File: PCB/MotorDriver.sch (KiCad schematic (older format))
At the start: 5 parts, among them U1 DRV8871DDA

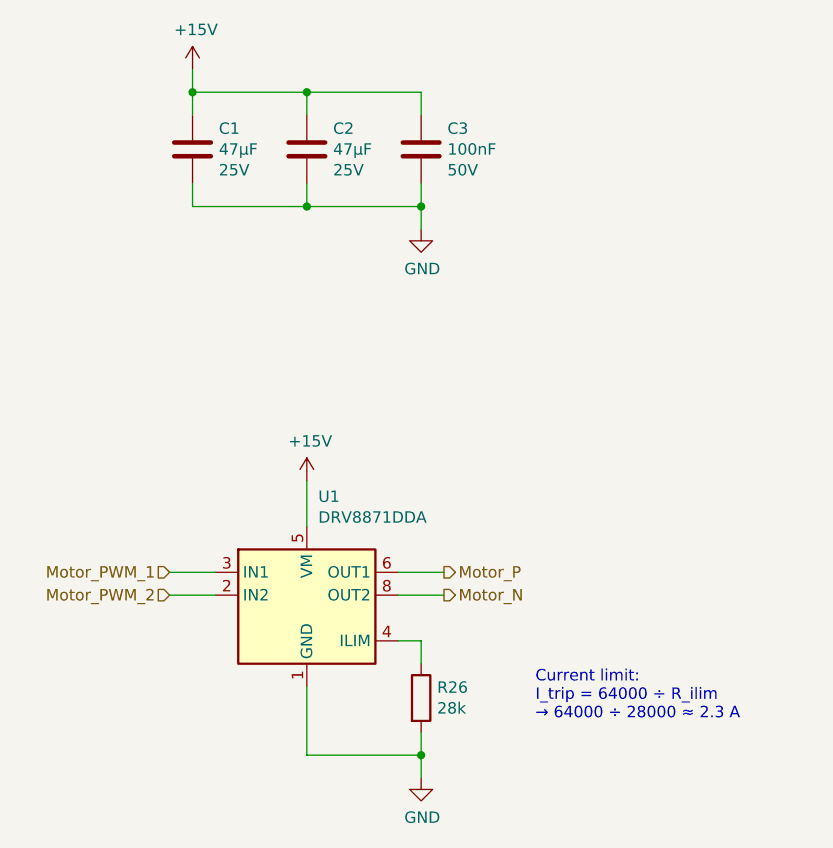
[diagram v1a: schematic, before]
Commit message: Add support for the weight sensor
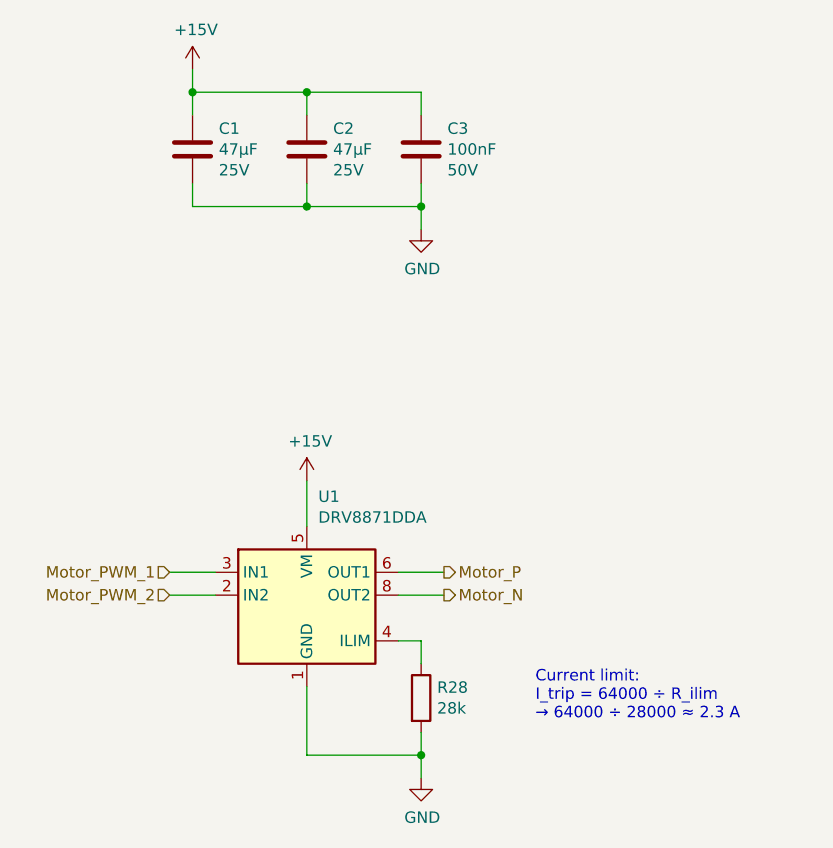
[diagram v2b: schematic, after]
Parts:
- renumbered R26 to R28
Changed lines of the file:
@@
 $Descr A4 11693 8268
 encoding utf-8
-Sheet 14 19
+Sheet 14 20
 Title "Litter Robot 3 - Motor driver"
-Date "2021-03-28"
+Date "2021-04-02"
 Rev "A1"
 Comp "L. Sartory"
@@
 	5500 3900 5500 3700
 $Comp
-L power:+15V #PWR049
+L power:+15V #PWR050
 U 1 1 60454ACA
 P 5500 3700
-F 0 "#PWR049" H 5500 3550 50  0001 C CNN
+F 0 "#PWR050" H 5500 3550 50  0001 C CNN
 F 1 "+15V" H 5515 3873 50  0000 C CNN
 F 2 "" H 5500 3700 50  0001 C CNN
@@
 $EndComp
 $Comp
-L power:+15V #PWR048
+L power:+15V #PWR049
 U 1 1 60457C46
 P 5000 1900
-F 0 "#PWR048" H 5000 1750 50  0001 C CNN
+F 0 "#PWR049" H 5000 1750 50  0001 C CNN
 F 1 "+15V" H 5015 2073 50  0000 C CNN
 F 2 "" H 5000 1900 50  0001 C CNN
@@
 $EndComp
 $Comp
-L power:GND #PWR050
+L power:GND #PWR051
 U 1 1 604586C2
 P 6000 2600
-F 0 "#PWR050" H 6000 2350 50  0001 C CNN
+F 0 "#PWR051" H 6000 2350 50  0001 C CNN
 F 1 "GND" H 6005 2427 50  0000 C CNN
 F 2 "" H 6000 2600 50  0001 C CNN
@@
 	5900 4200 6100 4200
 $Comp
-L power:GND #PWR051
+L power:GND #PWR052
 U 1 1 6046463F
 P 6000 5000
-F 0 "#PWR051" H 6000 4750 50  0001 C CNN
+F 0 "#PWR052" H 6000 4750 50  0001 C CNN
 F 1 "GND" H 6005 4827 50  0000 C CNN
 F 2 "" H 6000 5000 50  0001 C CNN
@@
 	6000 4400 6000 4500
 $Comp
-L Device:R R26
+L Device:R R28
 U 1 1 604667F9
 P 6000 4650
-F 0 "R26" H 6070 4696 50  0000 L CNN
+F 0 "R28" H 6070 4696 50  0000 L CNN
 F 1 "28k" H 6070 4605 50  0000 L CNN
 F 2 "Resistor_SMD:R_0603_1608Metric" V 5930 4650 50  0001 C CNN

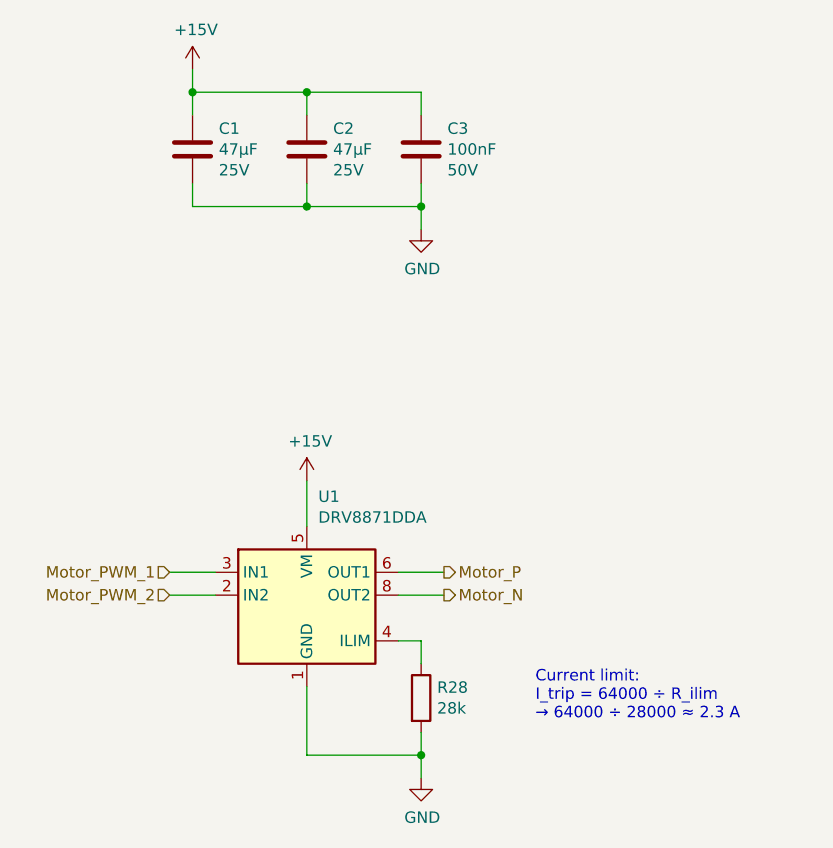
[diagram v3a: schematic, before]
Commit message: Re-annotate all components
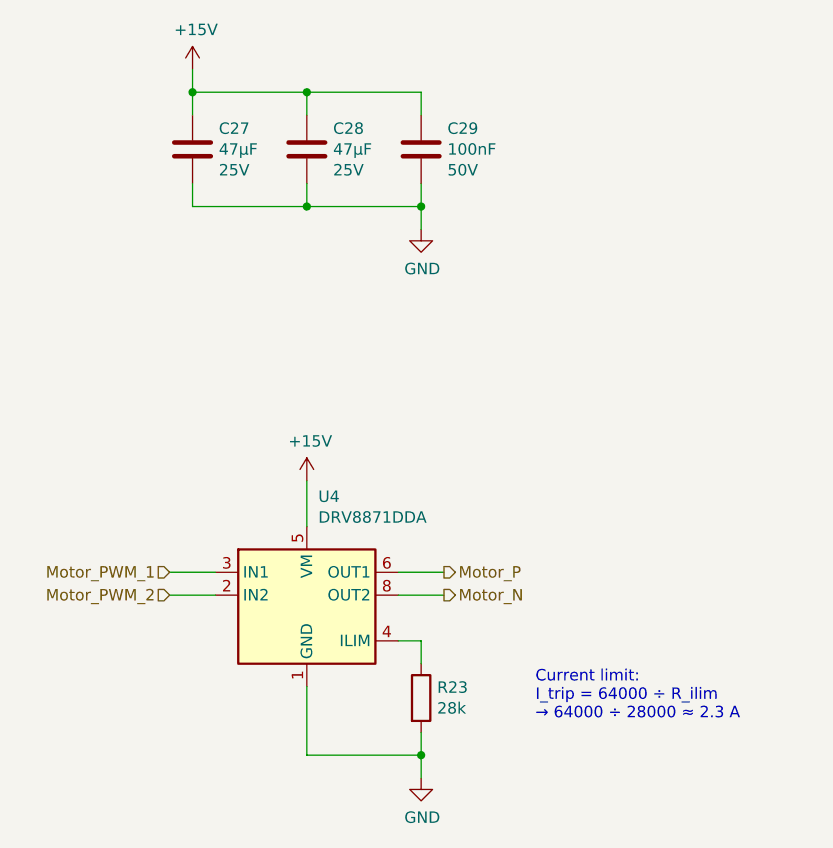
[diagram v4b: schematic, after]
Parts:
- renumbered C1 to C27, C2 to C28, C3 to C29, R28 to R23, U1 to U4
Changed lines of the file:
@@
 $Descr A4 11693 8268
 encoding utf-8
-Sheet 14 22
+Sheet 7 22
 Title "Litter Robot 3 - Motor driver"
-Date "2021-04-03"
+Date "2021-04-05"
 Rev "A1"
 Comp "L. Sartory"
@@
 $EndDescr
 $Comp
-L Device:C C3
+L Device:C C29
 U 1 1 6044E535
 P 6000 2250
-F 0 "C3" H 6115 2341 50  0000 L CNN
+F 0 "C29" H 6115 2341 50  0000 L CNN
 F 1 "100nF" H 6115 2250 50  0000 L CNN
 F 2 "Capacitor_SMD:C_0603_1608Metric" H 6038 2100 50  0001 C CNN
@@
 $EndComp
 $Comp
-L Device:C C1
+L Device:C C27
 U 1 1 60452EC0
 P 5000 2250
-F 0 "C1" H 5115 2341 50  0000 L CNN
+F 0 "C27" H 5115 2341 50  0000 L CNN
 F 1 "47µF" H 5115 2250 50  0000 L CNN
 F 2 "Capacitor_SMD:C_0603_1608Metric" H 5038 2100 50  0001 C CNN
@@
 $EndComp
 $Comp
-L Device:C C2
+L Device:C C28
 U 1 1 6045368C
 P 5500 2250
-F 0 "C2" H 5615 2341 50  0000 L CNN
+F 0 "C28" H 5615 2341 50  0000 L CNN
 F 1 "47µF" H 5615 2250 50  0000 L CNN
 F 2 "Capacitor_SMD:C_0603_1608Metric" H 5538 2100 50  0001 C CNN
@@
 	5500 3900 5500 3700
 $Comp
-L power:+15V #PWR050
+L power:+15V #PWR073
 U 1 1 60454ACA
 P 5500 3700
-F 0 "#PWR050" H 5500 3550 50  0001 C CNN
+F 0 "#PWR073" H 5500 3550 50  0001 C CNN
 F 1 "+15V" H 5515 3873 50  0000 C CNN
 F 2 "" H 5500 3700 50  0001 C CNN
@@
 $EndComp
 $Comp
-L power:+15V #PWR049
+L power:+15V #PWR071
 U 1 1 60457C46
 P 5000 1900
-F 0 "#PWR049" H 5000 1750 50  0001 C CNN
+F 0 "#PWR071" H 5000 1750 50  0001 C CNN
 F 1 "+15V" H 5015 2073 50  0000 C CNN
 F 2 "" H 5000 1900 50  0001 C CNN
@@
 $EndComp
 $Comp
-L power:GND #PWR051
+L power:GND #PWR072
 U 1 1 604586C2
 P 6000 2600
-F 0 "#PWR051" H 6000 2350 50  0001 C CNN
+F 0 "#PWR072" H 6000 2350 50  0001 C CNN
 F 1 "GND" H 6005 2427 50  0000 C CNN
 F 2 "" H 6000 2600 50  0001 C CNN
@@
 	5900 4200 6100 4200
 $Comp
-L power:GND #PWR052
+L power:GND #PWR074
 U 1 1 6046463F
 P 6000 5000
-F 0 "#PWR052" H 6000 4750 50  0001 C CNN
+F 0 "#PWR074" H 6000 4750 50  0001 C CNN
 F 1 "GND" H 6005 4827 50  0000 C CNN
 F 2 "" H 6000 5000 50  0001 C CNN
@@
 	6000 4400 6000 4500
 $Comp
-L Device:R R28
+L Device:R R23
 U 1 1 604667F9
 P 6000 4650
-F 0 "R28" H 6070 4696 50  0000 L CNN
+F 0 "R23" H 6070 4696 50  0000 L CNN
 F 1 "28k" H 6070 4605 50  0000 L CNN
 F 2 "Resistor_SMD:R_0603_1608Metric" V 5930 4650 50  0001 C CNN
@@
 Current limit:\nI_trip = 64000 ÷ R_ilim\n→ 64000 ÷ 28000 ≈ 2.3 A
 $Comp
-L Driver_Motor:DRV8871DDA U1
+L Driver_Motor:DRV8871DDA U4
 U 1 1 6044D886
 P 5500 4200
-F 0 "U1" H 5550 4631 50  0000 L CNN
+F 0 "U4" H 5550 4631 50  0000 L CNN
 F 1 "DRV8871DDA" H 5550 4540 50  0000 L CNN
 F 2 "Package_SO:Texas_HTSOP-8-1EP_3.9x4.9mm_P1.27mm_EP2.95x4.9mm_Mask2.4x3.1mm_ThermalVias" H 5750 4150 50  0001 C CNN

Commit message: Change the higher value capacitors to 1206
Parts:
- C27, C28: footprint Capacitor_SMD:C_0603_1608Metric -> Capacitor_SMD:C_1206_3216Metric
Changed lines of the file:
@@
 F 0 "C27" H 5115 2341 50  0000 L CNN
 F 1 "47µF" H 5115 2250 50  0000 L CNN
-F 2 "Capacitor_SMD:C_0603_1608Metric" H 5038 2100 50  0001 C CNN
+F 2 "Capacitor_SMD:C_1206_3216Metric" H 5038 2100 50  0001 C CNN
 F 3 "https://product.tdk.com/system/files/dam/doc/product/capacitor/ceramic/mlcc/catalog/mlcc_commercial_general_en.pdf" H 5000 2250 50  0001 C CNN
 F 4 "25V" H 5115 2159 50  0000 L CNN "Voltage"
@@
 F 0 "C28" H 5615 2341 50  0000 L CNN
 F 1 "47µF" H 5615 2250 50  0000 L CNN
-F 2 "Capacitor_SMD:C_0603_1608Metric" H 5538 2100 50  0001 C CNN
+F 2 "Capacitor_SMD:C_1206_3216Metric" H 5538 2100 50  0001 C CNN
 F 3 "https://product.tdk.com/system/files/dam/doc/product/capacitor/ceramic/mlcc/catalog/mlcc_commercial_general_en.pdf" H 5500 2250 50  0001 C CNN
 F 4 "25V" H 5615 2159 50  0000 L CNN "Voltage"

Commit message: Adapt the DRV8871 footprint for the PCB constraints
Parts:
- U4: footprint Package_SO:Texas_HTSOP-8-1EP_3.9x4.9mm_P1.27mm_EP2.95x4.9mm_Mask2.4x3.1mm_ThermalVias -> LitterRobot:Texas_DRV8871
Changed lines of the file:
@@
 F 0 "U4" H 5550 4631 50  0000 L CNN
 F 1 "DRV8871DDA" H 5550 4540 50  0000 L CNN
-F 2 "Package_SO:Texas_HTSOP-8-1EP_3.9x4.9mm_P1.27mm_EP2.95x4.9mm_Mask2.4x3.1mm_ThermalVias" H 5750 4150 50  0001 C CNN
+F 2 "LitterRobot:Texas_DRV8871" H 5750 4150 50  0001 C CNN
 F 3 "http://www.ti.com/lit/ds/symlink/drv8871.pdf" H 5750 4150 50  0001 C CNN
 F 4 "DRV8871DDARQ1" H 5500 4200 50  0001 C CNN "Part_number"

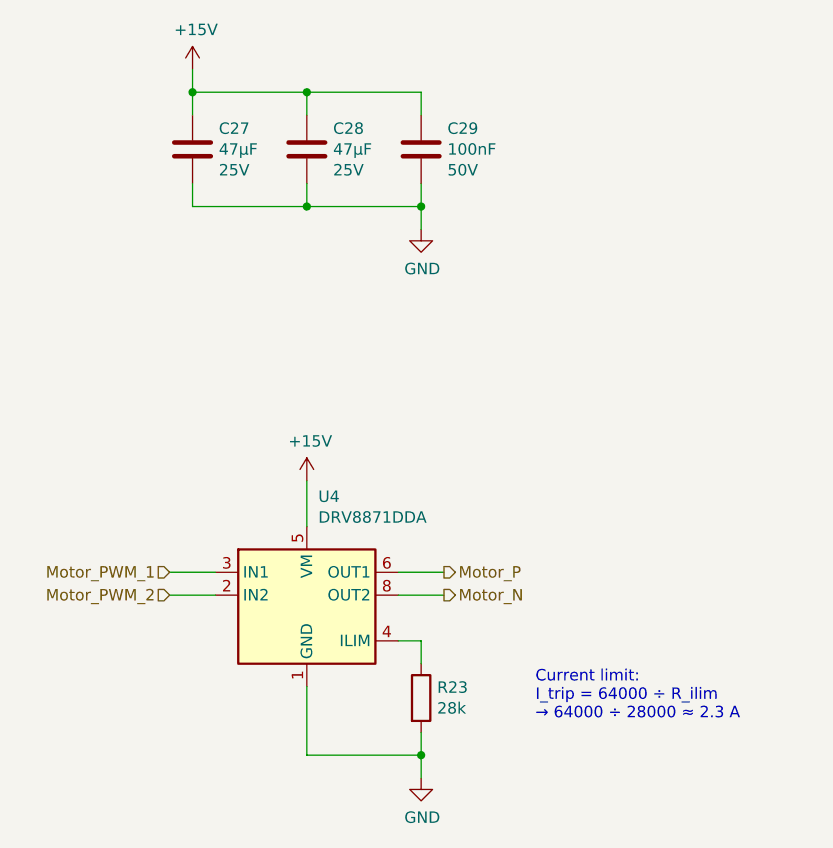
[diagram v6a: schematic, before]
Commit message: Add the EMB1061 Bluetooth module
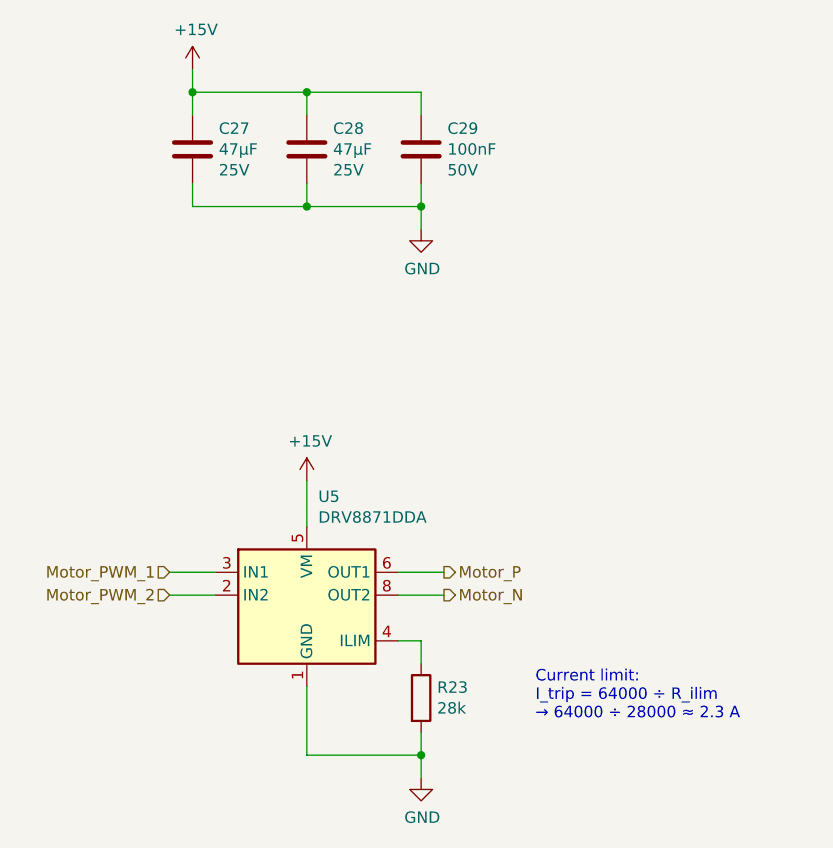
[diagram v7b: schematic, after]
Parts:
- renumbered U4 to U5
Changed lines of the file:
@@
 $Descr A4 11693 8268
 encoding utf-8
-Sheet 7 22
+Sheet 7 23
 Title "Litter Robot 3 - Motor driver"
-Date "2021-04-05"
+Date "2021-04-10"
 Rev "A1"
 Comp "L. Sartory"
@@
 	5500 3900 5500 3700
 $Comp
-L power:+15V #PWR073
+L power:+15V #PWR076
 U 1 1 60454ACA
 P 5500 3700
-F 0 "#PWR073" H 5500 3550 50  0001 C CNN
+F 0 "#PWR076" H 5500 3550 50  0001 C CNN
 F 1 "+15V" H 5515 3873 50  0000 C CNN
 F 2 "" H 5500 3700 50  0001 C CNN
@@
 $EndComp
 $Comp
-L power:+15V #PWR071
+L power:+15V #PWR074
 U 1 1 60457C46
 P 5000 1900
-F 0 "#PWR071" H 5000 1750 50  0001 C CNN
+F 0 "#PWR074" H 5000 1750 50  0001 C CNN
 F 1 "+15V" H 5015 2073 50  0000 C CNN
 F 2 "" H 5000 1900 50  0001 C CNN
@@
 $EndComp
 $Comp
-L power:GND #PWR072
+L power:GND #PWR075
 U 1 1 604586C2
 P 6000 2600
-F 0 "#PWR072" H 6000 2350 50  0001 C CNN
+F 0 "#PWR075" H 6000 2350 50  0001 C CNN
 F 1 "GND" H 6005 2427 50  0000 C CNN
 F 2 "" H 6000 2600 50  0001 C CNN
@@
 	5900 4200 6100 4200
 $Comp
-L power:GND #PWR074
+L power:GND #PWR077
 U 1 1 6046463F
 P 6000 5000
-F 0 "#PWR074" H 6000 4750 50  0001 C CNN
+F 0 "#PWR077" H 6000 4750 50  0001 C CNN
 F 1 "GND" H 6005 4827 50  0000 C CNN
 F 2 "" H 6000 5000 50  0001 C CNN
@@
 Current limit:\nI_trip = 64000 ÷ R_ilim\n→ 64000 ÷ 28000 ≈ 2.3 A
 $Comp
-L Driver_Motor:DRV8871DDA U4
+L Driver_Motor:DRV8871DDA U5
 U 1 1 6044D886
 P 5500 4200
-F 0 "U4" H 5550 4631 50  0000 L CNN
+F 0 "U5" H 5550 4631 50  0000 L CNN
 F 1 "DRV8871DDA" H 5550 4540 50  0000 L CNN
 F 2 "LitterRobot:Texas_DRV8871" H 5750 4150 50  0001 C CNN
